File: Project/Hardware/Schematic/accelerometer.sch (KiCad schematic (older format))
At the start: 2 parts

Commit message: Fixa bibliotek ref
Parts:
- removed U?: lis3dh_board, symbol lab-rescue:lis3dh_board-PASC
- added U?: lis3dh_board, symbol PASC:lis3dh_board
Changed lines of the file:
@@
 Wire Wire Line
 	6200 2950 6200 3150
-$Comp
-L lab-rescue:lis3dh_board-PASC U?
-U 1 1 5C59F00B
-P 7350 3350
-F 0 "U?" H 7350 3825 50  0000 C CNN
-F 1 "lis3dh_board" H 7350 3734 50  0000 C CNN
-F 2 "" H 7350 3350 50  0001 C CNN
-F 3 "" H 7350 3350 50  0001 C CNN
-	1    7350 3350
-	1    0    0    -1
-$EndComp
 Wire Wire Line
 	6700 3150 6200 3150
@@
 Text HLabel 8000 3550 2    50   Input ~ 0
 CS_INT
+$Comp
+L PASC:lis3dh_board U?
+U 1 1 5C5E039C
+P 7350 3350
+F 0 "U?" H 7350 3825 50  0000 C CNN
+F 1 "lis3dh_board" H 7350 3734 50  0000 C CNN
+F 2 "" H 7350 3350 50  0001 C CNN
+F 3 "" H 7350 3350 50  0001 C CNN
+	1    7350 3350
+	1    0    0    -1
+$EndComp
 $EndSCHEMATC

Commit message: Lcd bb (#12)
* Tagit bort knapp, ändrat power till piezo
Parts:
- U?: footprint (none) -> PASC:LIS3DH
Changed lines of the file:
@@
 $EndDescr
 $Comp
-L power:+3.3V #PWR0120
+L power:+3.3V #PWR?
 U 1 1 5C5AB0A3
 P 6200 2950
-F 0 "#PWR0120" H 6200 2800 50  0001 C CNN
+F 0 "#PWR?" H 6200 2800 50  0001 C CNN
 F 1 "+3.3V" H 6215 3123 50  0000 C CNN
 F 2 "" H 6200 2950 50  0001 C CNN
@@
 F 0 "U?" H 7350 3825 50  0000 C CNN
 F 1 "lis3dh_board" H 7350 3734 50  0000 C CNN
-F 2 "" H 7350 3350 50  0001 C CNN
+F 2 "PASC:LIS3DH" H 7350 3350 50  0001 C CNN
 F 3 "" H 7350 3350 50  0001 C CNN
 	1    7350 3350

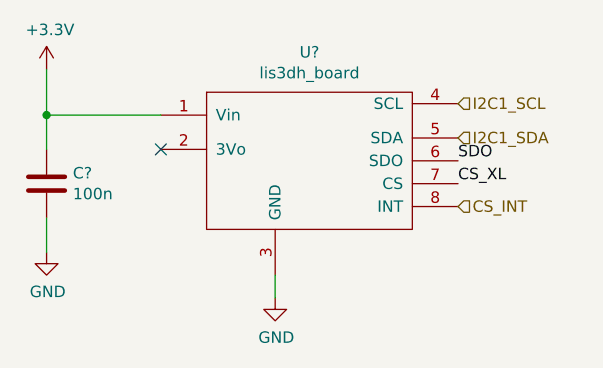
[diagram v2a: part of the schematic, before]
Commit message: Tog bort power supply +7, lade till switch för att switcha mellan batteri och USB power. Lade till power-net symbol för oregulerad supply voltage +VIN.
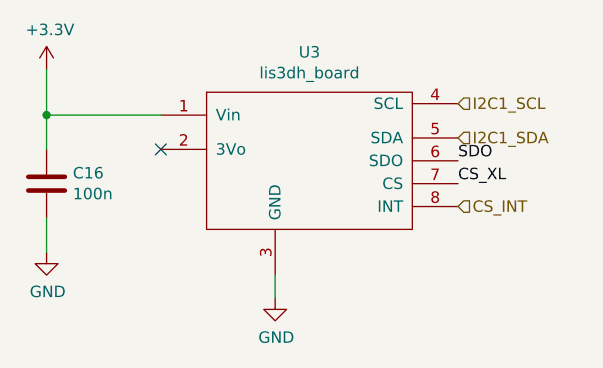
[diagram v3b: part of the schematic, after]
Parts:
- gave numbers to parts that had none: 2
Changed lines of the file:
@@
 $EndDescr
 $Comp
-L power:+3.3V #PWR?
+L power:+3.3V #PWR0120
 U 1 1 5C5AB0A3
 P 6200 2950
-F 0 "#PWR?" H 6200 2800 50  0001 C CNN
+F 0 "#PWR0120" H 6200 2800 50  0001 C CNN
 F 1 "+3.3V" H 6215 3123 50  0000 C CNN
 F 2 "" H 6200 2950 50  0001 C CNN
@@
 	6700 3150 6200 3150
 $Comp
-L power:GND #PWR?
+L power:GND #PWR0121
 U 1 1 5C59F3FC
 P 7200 3950
-F 0 "#PWR?" H 7200 3700 50  0001 C CNN
+F 0 "#PWR0121" H 7200 3700 50  0001 C CNN
 F 1 "GND" H 7205 3777 50  0000 C CNN
 F 2 "" H 7200 3950 50  0001 C CNN
@@
 	7200 3850 7200 3950
 $Comp
-L power:GND #PWR?
+L power:GND #PWR0122
 U 1 1 5C59F76F
 P 9000 3600
-F 0 "#PWR?" H 9000 3350 50  0001 C CNN
+F 0 "#PWR0122" H 9000 3350 50  0001 C CNN
 F 1 "GND" H 9005 3427 50  0000 C CNN
 F 2 "" H 9000 3600 50  0001 C CNN
@@
 NoConn ~ 6700 3300
 $Comp
-L Device:C C?
+L Device:C C16
 U 1 1 5C5A61DB
 P 6200 3450
-F 0 "C?" H 6315 3496 50  0000 L CNN
+F 0 "C16" H 6315 3496 50  0000 L CNN
 F 1 "100n" H 6315 3405 50  0000 L CNN
 F 2 "" H 6238 3300 50  0001 C CNN
@@
 $EndComp
 $Comp
-L power:GND #PWR?
+L power:GND #PWR0123
 U 1 1 5C5A62A1
 P 6200 3750
-F 0 "#PWR?" H 6200 3500 50  0001 C CNN
+F 0 "#PWR0123" H 6200 3500 50  0001 C CNN
 F 1 "GND" H 6205 3577 50  0000 C CNN
 F 2 "" H 6200 3750 50  0001 C CNN
@@
 CS_XL
 $Comp
-L power:+3V3 #PWR?
+L power:+3V3 #PWR0124
 U 1 1 5C5D1727
 P 9000 3000
-F 0 "#PWR?" H 9000 2850 50  0001 C CNN
+F 0 "#PWR0124" H 9000 2850 50  0001 C CNN
 F 1 "+3V3" H 9015 3173 50  0000 C CNN
 F 2 "" H 9000 3000 50  0001 C CNN
@@
 CS_INT
 $Comp
-L PASC:lis3dh_board U?
+L PASC:lis3dh_board U3
 U 1 1 5C5E039C
 P 7350 3350
-F 0 "U?" H 7350 3825 50  0000 C CNN
+F 0 "U3" H 7350 3825 50  0000 C CNN
 F 1 "lis3dh_board" H 7350 3734 50  0000 C CNN
 F 2 "PASC:LIS3DH" H 7350 3350 50  0001 C CNN

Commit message: Intermediate...
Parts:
- C16: footprint (none) -> Capacitor_SMD:C_0805_2012Metric_Pad1.15x1.40mm_HandSolder
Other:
- moved on the sheet: C16, U3
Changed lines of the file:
@@
 EELAYER 26 0
 EELAYER END
-$Descr A4 11693 8268
+$Descr User 5512 5512
 encoding utf-8
 Sheet 2 7
 Title ""
-Date ""
-Rev ""
-Comp ""
+Date "2019-02-12"
+Rev "1"
+Comp "PASC"
 Comment1 ""
 Comment2 ""
@@
 L power:+3.3V #PWR0120
 U 1 1 5C5AB0A3
-P 6200 2950
-F 0 "#PWR0120" H 6200 2800 50  0001 C CNN
-F 1 "+3.3V" H 6215 3123 50  0000 C CNN
-F 2 "" H 6200 2950 50  0001 C CNN
-F 3 "" H 6200 2950 50  0001 C CNN
-	1    6200 2950
+P 1300 1850
+F 0 "#PWR0120" H 1300 1700 50  0001 C CNN
+F 1 "+3.3V" H 1315 2023 50  0000 C CNN
+F 2 "" H 1300 1850 50  0001 C CNN
+F 3 "" H 1300 1850 50  0001 C CNN
+	1    1300 1850
 	1    0    0    -1
 $EndComp
 Wire Wire Line
-	6200 2950 6200 3150
+	1300 1850 1300 2050
 Wire Wire Line
-	6700 3150 6200 3150
+	1800 2050 1300 2050
 $Comp
 L power:GND #PWR0121
 U 1 1 5C59F3FC
-P 7200 3950
-F 0 "#PWR0121" H 7200 3700 50  0001 C CNN
-F 1 "GND" H 7205 3777 50  0000 C CNN
-F 2 "" H 7200 3950 50  0001 C CNN
-F 3 "" H 7200 3950 50  0001 C CNN
-	1    7200 3950
+P 2300 2850
+F 0 "#PWR0121" H 2300 2600 50  0001 C CNN
+F 1 "GND" H 2305 2677 50  0000 C CNN
+F 2 "" H 2300 2850 50  0001 C CNN
+F 3 "" H 2300 2850 50  0001 C CNN
+	1    2300 2850
 	1    0    0    -1
 $EndComp
 Wire Wire Line
-	7200 3850 7200 3950
+	2300 2750 2300 2850
 $Comp
 L power:GND #PWR0122
 U 1 1 5C59F76F
-P 9000 3600
-F 0 "#PWR0122" H 9000 3350 50  0001 C CNN
-F 1 "GND" H 9005 3427 50  0000 C CNN
-F 2 "" H 9000 3600 50  0001 C CNN
-F 3 "" H 9000 3600 50  0001 C CNN
-	1    9000 3600
+P 4100 2500
+F 0 "#PWR0122" H 4100 2250 50  0001 C CNN
+F 1 "GND" H 4105 2327 50  0000 C CNN
+F 2 "" H 4100 2500 50  0001 C CNN
+F 3 "" H 4100 2500 50  0001 C CNN
+	1    4100 2500
 	1    0    0    -1
 $EndComp
-NoConn ~ 6700 3300
+NoConn ~ 1800 2200
 $Comp
 L Device:C C16
 U 1 1 5C5A61DB
-P 6200 3450
-F 0 "C16" H 6315 3496 50  0000 L CNN
-F 1 "100n" H 6315 3405 50  0000 L CNN
-F 2 "" H 6238 3300 50  0001 C CNN
-F 3 "~" H 6200 3450 50  0001 C CNN
-	1    6200 3450
+P 1300 2350
+F 0 "C16" H 1415 2396 50  0000 L CNN
+F 1 "100n" H 1415 2305 50  0000 L CNN
+F 2 "Capacitor_SMD:C_0805_2012Metric_Pad1.15x1.40mm_HandSolder" H 1338 2200 50  0001 C CNN
+F 3 "~" H 1300 2350 50  0001 C CNN
+	1    1300 2350
 	1    0    0    -1
 $EndComp
@@
 L power:GND #PWR0123
 U 1 1 5C5A62A1
-P 6200 3750
-F 0 "#PWR0123" H 6200 3500 50  0001 C CNN
-F 1 "GND" H 6205 3577 50  0000 C CNN
-F 2 "" H 6200 3750 50  0001 C CNN
-F 3 "" H 6200 3750 50  0001 C CNN
-	1    6200 3750
+P 1300 2650
+F 0 "#PWR0123" H 1300 2400 50  0001 C CNN
+F 1 "GND" H 1305 2477 50  0000 C CNN
+F 2 "" H 1300 2650 50  0001 C CNN
+F 3 "" H 1300 2650 50  0001 C CNN
+	1    1300 2650
 	1    0    0    -1
 $EndComp
 Wire Wire Line
-	6200 3150 6200 3300
-Connection ~ 6200 3150
+	1300 2050 1300 2200
+Connection ~ 1300 2050
 Wire Wire Line
-	6200 3600 6200 3750
-Text Notes 9050 3550 0    50   ~ 0
+	1300 2500 1300 2650
+Text Notes 4150 2450 0    50   ~ 0
 I2C Address: 0x18
-Text Label 8000 3350 0    50   ~ 0
+Text Label 3100 2250 0    50   ~ 0
 SDO
 Wire Wire Line
-	9000 3400 8900 3400
+	4100 2300 4000 2300
 Wire Wire Line
-	9000 3400 9000 3600
-Text Label 8900 3400 2    50   ~ 0
+	4100 2300 4100 2500
+Text Label 4000 2300 2    50   ~ 0
 SDO
-Text Label 8000 3450 0    50   ~ 0
+Text Label 3100 2350 0    50   ~ 0
 CS_XL
 $Comp
 L power:+3V3 #PWR0124
 U 1 1 5C5D1727
-P 9000 3000
-F 0 "#PWR0124" H 9000 2850 50  0001 C CNN
-F 1 "+3V3" H 9015 3173 50  0000 C CNN
-F 2 "" H 9000 3000 50  0001 C CNN
-F 3 "" H 9000 3000 50  0001 C CNN
-	1    9000 3000
+P 4100 1900
+F 0 "#PWR0124" H 4100 1750 50  0001 C CNN
+F 1 "+3V3" H 4115 2073 50  0000 C CNN
+F 2 "" H 4100 1900 50  0001 C CNN
+F 3 "" H 4100 1900 50  0001 C CNN
+	1    4100 1900
 	1    0    0    -1
 $EndComp
 Wire Wire Line
-	9000 3000 9000 3200
+	4100 1900 4100 2100
 Wire Wire Line
-	9000 3200 8900 3200
-Text Label 8900 3200 2    50   ~ 0
+	4100 2100 4000 2100
+Text Label 4000 2100 2    50   ~ 0
 CS_XL
-Text Notes 9050 3200 0    50   ~ 0
+Text Notes 4150 2100 0    50   ~ 0
 Use I2C.
-Text HLabel 8000 3100 2    50   Input ~ 0
+Text HLabel 3100 2000 2    50   Input ~ 0
 I2C1_SCL
-Text HLabel 8000 3250 2    50   Input ~ 0
+Text HLabel 3100 2150 2    50   Input ~ 0
 I2C1_SDA
-Text HLabel 8000 3550 2    50   Input ~ 0
+Text HLabel 3100 2450 2    50   Input ~ 0
 CS_INT
 $Comp
 L PASC:lis3dh_board U3
 U 1 1 5C5E039C
-P 7350 3350
-F 0 "U3" H 7350 3825 50  0000 C CNN
-F 1 "lis3dh_board" H 7350 3734 50  0000 C CNN
-F 2 "PASC:LIS3DH" H 7350 3350 50  0001 C CNN
-F 3 "" H 7350 3350 50  0001 C CNN
-	1    7350 3350
+P 2450 2250
+F 0 "U3" H 2450 2725 50  0000 C CNN
+F 1 "lis3dh_board" H 2450 2634 50  0000 C CNN
+F 2 "PASC:LIS3DH" H 2450 2250 50  0001 C CNN
+F 3 "" H 2450 2250 50  0001 C CNN
+	1    2450 2250
 	1    0    0    -1
 $EndComp
